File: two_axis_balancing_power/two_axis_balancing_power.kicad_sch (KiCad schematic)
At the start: 0 parts

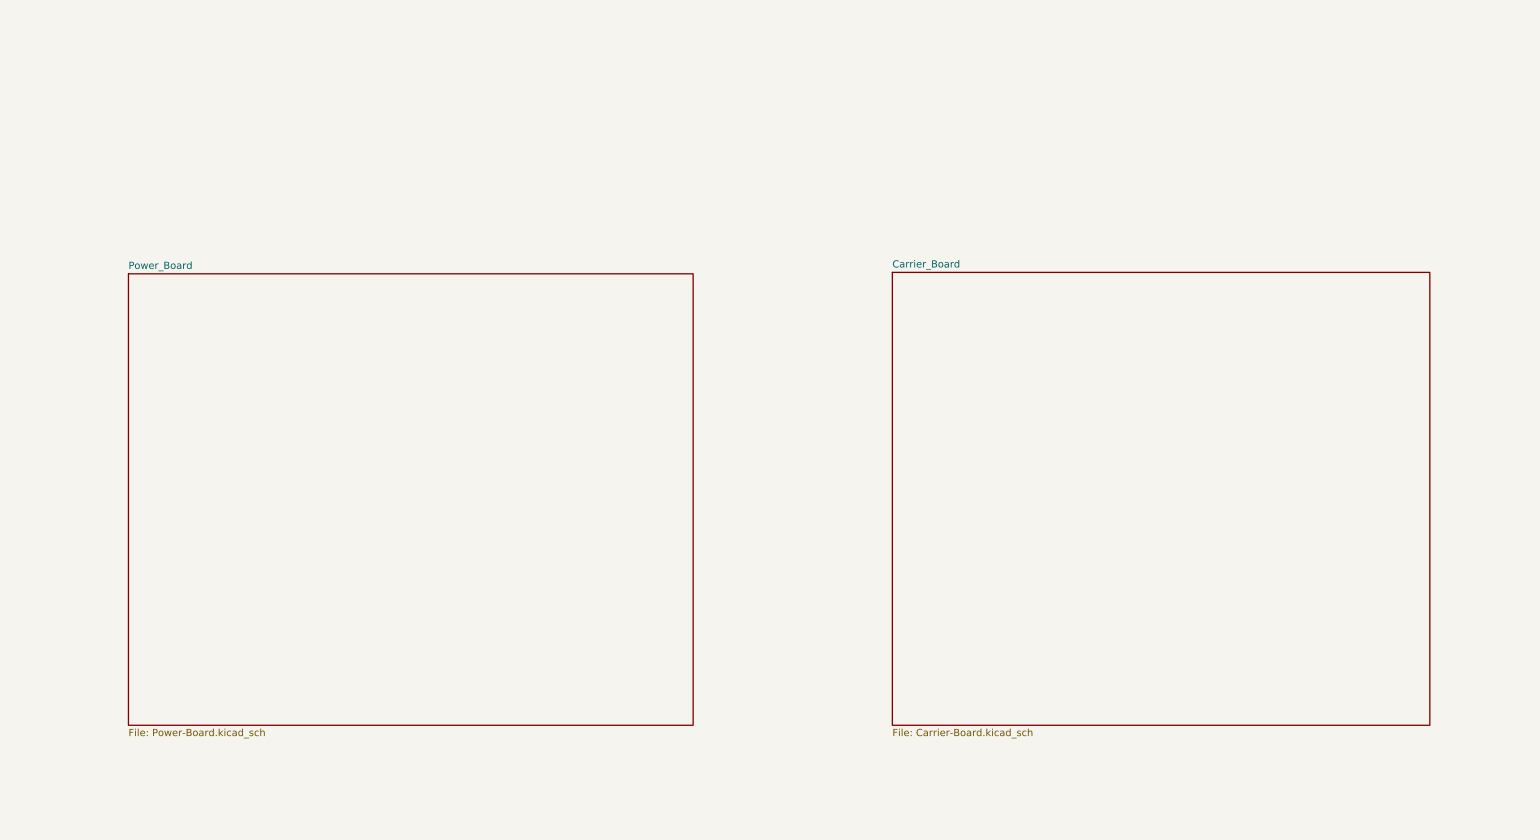
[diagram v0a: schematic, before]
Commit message: Fixed file structure
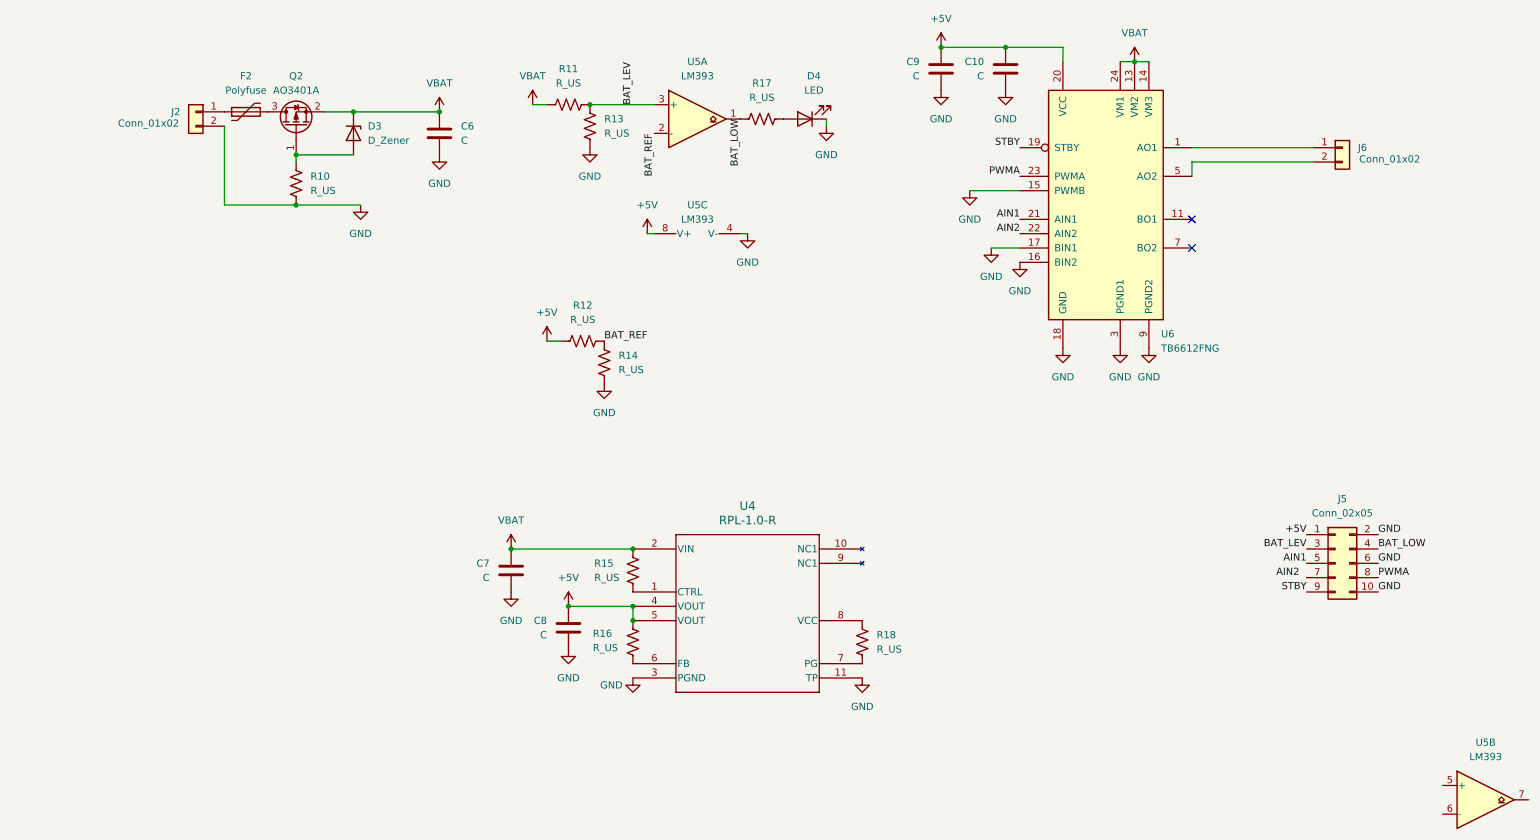
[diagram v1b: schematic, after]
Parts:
- added C10, C6, C7, C8, C9: C, symbol Device:C
- added D3: D_Zener, symbol Device:D_Zener
- added D4: LED, symbol Device:LED
- added F2: Polyfuse, symbol Device:Polyfuse
- added J2, J6: Conn_01x02, symbol Connector_Generic:Conn_01x02
- added J5: Conn_02x05, symbol Connector_Generic:Conn_02x05_Odd_Even
- added Q2: AO3401A, Package_TO_SOT_SMD:SOT-23, symbol Transistor_FET:AO3401A
- added R10, R11, R12, R13, R14, R15, R16, R17, R18: R_US, symbol Device:R_US
- added U4: RPL-1.0-R, 11L-LGA-M_RPL-1_RCP, symbol RPL_1.0:RPL-1.0-R
- added U5: LM393, symbol Comparator:LM393
- added U6: TB6612FNG, Package_SO:SSOP-24_5.3x8.2mm_P0.65mm, symbol Driver_Motor:TB6612FNG
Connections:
- new net: R16.1, U4.6 (FB)
- new net: R18.1, U4.8 (VCC)
- new net: R18.2, U4.7 (PG)
- new net: D4.2 (A), R17.1
- new net: R15.2, U4.1 (CTRL)
- new net: J6.1 (Pin_1), U6.1 (AO1), U6.2 (AO1)
- new net: U6.11 (BO1), U6.12 (BO1)
- new net: J6.2 (Pin_2), U6.5 (AO2), U6.6 (AO2)
- new net: U6.7 (BO2), U6.8 (BO2)
- new net: F2.1, J2.1 (Pin_1)
- new net: D3.2 (A), Q2.1 (G), R10.1
- new net: F2.2, Q2.3 (D)
- new net +5V: C10.2, C8.2, C9.2, J5.1 (Pin_1), R12.2, R16.2, U4.4 (VOUT), U4.5 (VOUT), U5.8 (V+), U6.20 (VCC)
- new net AIN1: J5.5 (Pin_5), U6.21 (AIN1)
- new net AIN2: U6.22 (AIN2)
- new net BAT_LEV: J5.3 (Pin_3), R11.1, R13.1, U5.3 (+)
- new net BAT_LOW: J5.4 (Pin_4), R17.2, U5.1
- new net BAT_REF: R12.1, R14.1, U5.2 (-)
- new net GND: C10.1, C6.2, C7.1, C8.1, C9.1, D4.1 (K), J2.2 (Pin_2), J5.10 (Pin_10), J5.2 (Pin_2), J5.6 (Pin_6), R10.2, R13.2, R14.2, U4.11 (TP), U4.3 (PGND), U5.4 (V-), U6.10 (PGND2), U6.15 (PWMB), U6.16 (BIN2), U6.17 (BIN1), U6.18 (GND), U6.3 (PGND1), U6.4 (PGND1), U6.9 (PGND2)
- new net PWMA: J5.8 (Pin_8), U6.23 (PWMA)
- new net STBY: J5.9 (Pin_9), U6.19 (STBY)
- new net VBAT: C6.1, C7.2, D3.1 (K), Q2.2 (S), R11.2, R15.1, U4.2 (VIN), U6.13 (VM2), U6.14 (VM3), U6.24 (VM1)
- no-connect marks 0 -> 2
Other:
- removed sheet Carrier_Board
- removed sheet Power_Board

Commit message: Finished topology
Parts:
- added J7: Conn_01x02, symbol Connector_Generic:Conn_01x02
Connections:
- net GND: now also J7.2 (Pin_2)
- net MOTOR_P: now reaches J6.1 (Pin_1), U6.1 (AO1), U6.2 (AO1)
- net MOTOR_N: now reaches J6.2 (Pin_2), U6.5 (AO2), U6.6 (AO2)
- net V_BAT_BYP: now reaches F2.1, J2.1 (Pin_1)
- net V_BAT_BYP: now also J7.1 (Pin_1)
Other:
- moved on the sheet: C6, D3, F2, J2, J5, J6, Q2, R10

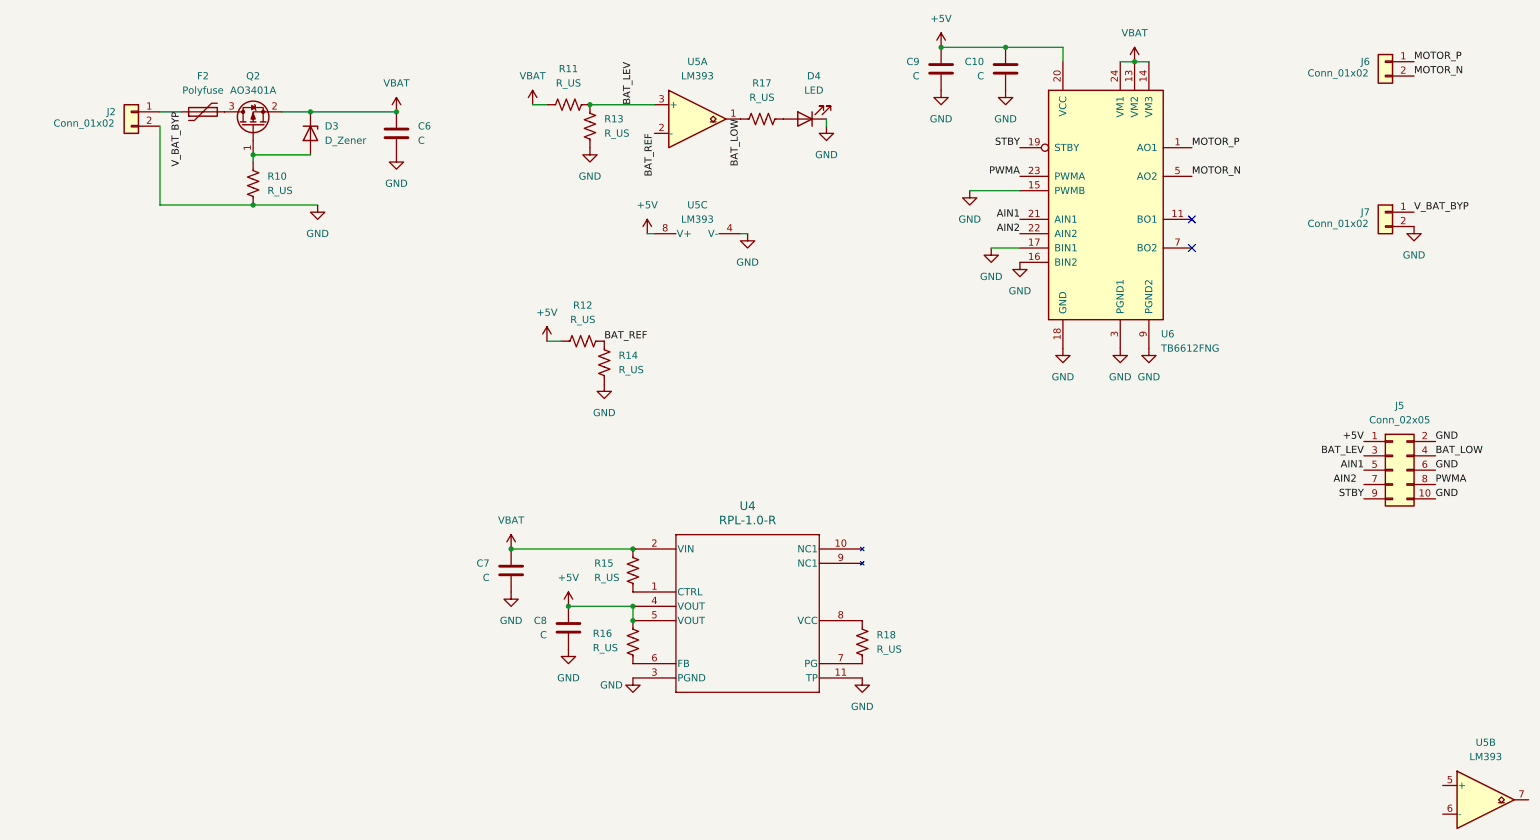
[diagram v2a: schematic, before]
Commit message: Sized passives
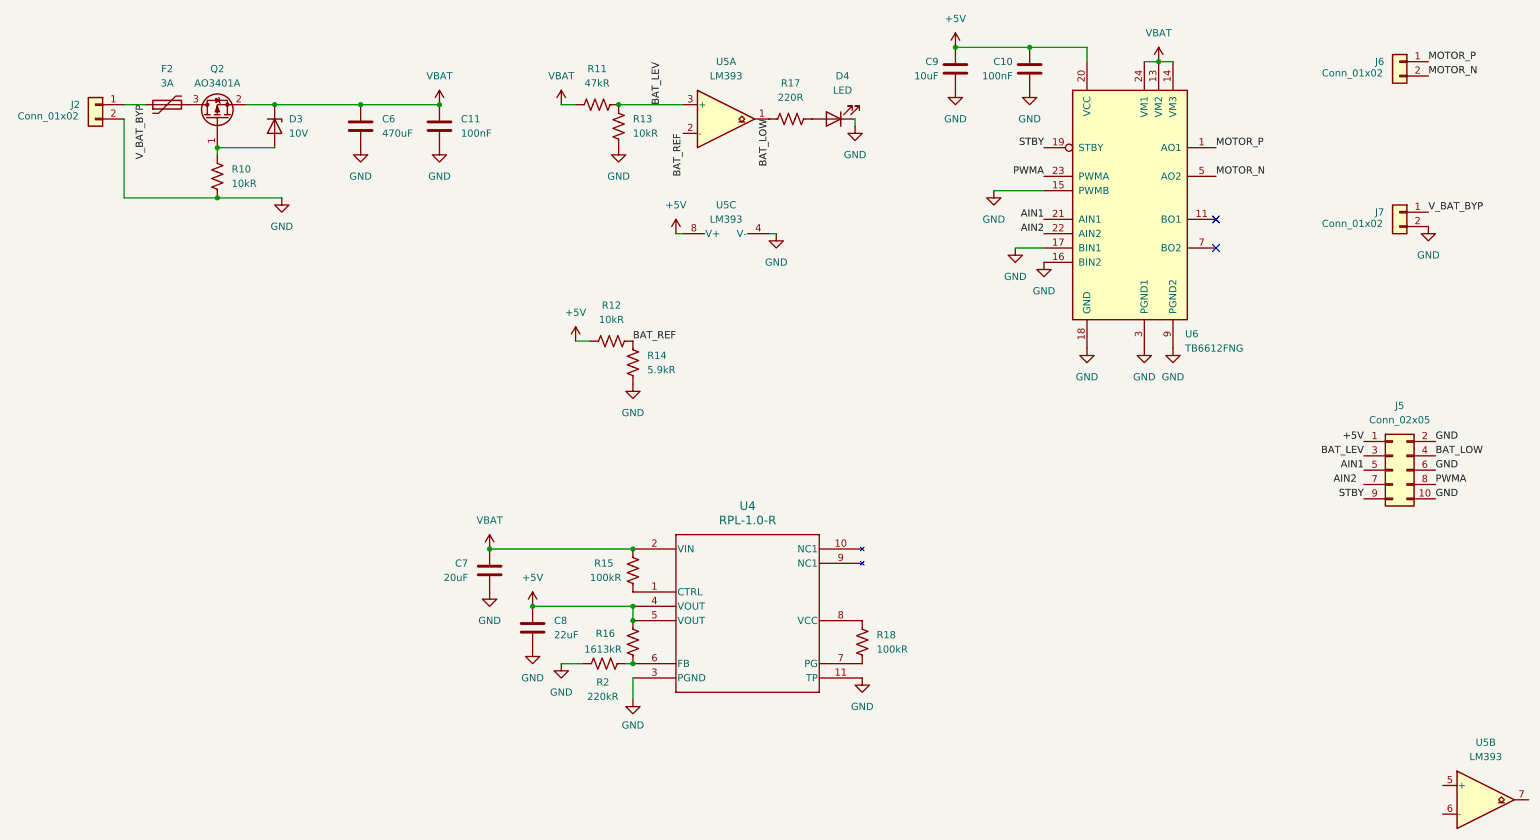
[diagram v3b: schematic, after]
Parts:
- added C11: 100nF, symbol Device:C
- added R2: 220kR, symbol Device:R_US
- C10: value C -> 100nF
- C6: value C -> 470uF
- C7: value C -> 20uF
- C8: value C -> 22uF
- C9: value C -> 10uF
- D3: value D_Zener -> 10V
- F2: value Polyfuse -> 3A
- R10, R12, R13: value R_US -> 10kR
- R11: value R_US -> 47kR
- R14: value R_US -> 5.9kR
- R15, R18: value R_US -> 100kR
- R16: value R_US -> 1613kR
- R17: value R_US -> 220R
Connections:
- net GND: now also C11.2, R2.1
- net VBAT: now also C11.1
- net at R16.1, U4.6 (FB): now also R2.2
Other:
- moved on the sheet: C10, C6, C7, C8, C9, D3, D4, F2, J2, J6, J7, Q2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

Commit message: Started pcb design
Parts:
- removed J7: Conn_01x02, symbol Connector_Generic:Conn_01x02
- C1: renamed from C6; footprint (none) -> Capacitor_SMD:C_0603_1608Metric
- C2: renamed from C11; footprint (none) -> Capacitor_SMD:C_0603_1608Metric
- C3: renamed from C7; footprint (none) -> Capacitor_SMD:C_0603_1608Metric
- C4: renamed from C8; footprint (none) -> Capacitor_SMD:C_0603_1608Metric
- C5: renamed from C9; footprint (none) -> Capacitor_SMD:C_0603_1608Metric
- C6: renamed from C10; footprint (none) -> Capacitor_SMD:C_0603_1608Metric
- D1: renamed from D3; footprint (none) -> Diode_SMD:D_SOD-123
- D2: renamed from D4; footprint (none) -> LED_SMD:LED_0603_1608Metric
- F1: renamed from F2; footprint (none) -> Fuse:Fuse_1812_4532Metric
- J1: renamed from J2; footprint (none) -> Connector_AMASS:AMASS_XT60-M_1x02_P7.20mm_Vertical
- J2: renamed from J5; footprint (none) -> Connector_IDC:IDC-Header_2x05_P2.54mm_Vertical
- J3: renamed from J6; footprint (none) -> Connector_JST:JST_XH_S2B-XH-A_1x02_P2.50mm_Horizontal
- R1: renamed from R10; footprint (none) -> Resistor_SMD:R_0603_1608Metric
- R10: renamed from R18; footprint (none) -> Resistor_SMD:R_0603_1608Metric
- R2: renamed from R11; footprint (none) -> Resistor_SMD:R_0603_1608Metric
- R3: renamed from R2; footprint (none) -> Resistor_SMD:R_0603_1608Metric
- R4: renamed from R12; footprint (none) -> Resistor_SMD:R_0603_1608Metric
- R5: renamed from R13; footprint (none) -> Resistor_SMD:R_0603_1608Metric
- R6: renamed from R14; footprint (none) -> Resistor_SMD:R_0603_1608Metric
- R7: renamed from R15; footprint (none) -> Resistor_SMD:R_0603_1608Metric
- R8: renamed from R16; footprint (none) -> Resistor_SMD:R_0603_1608Metric
- R9: renamed from R17; footprint (none) -> Resistor_SMD:R_0603_1608Metric
- U1: renamed from U4; footprint 11L-LGA-M_RPL-1_RCP -> RCL-1:11L-LGA-M_RPL-1_RCP
- U2: renamed from U5; footprint (none) -> Package_SO:SOIC-8_3.9x4.9mm_P1.27mm
- renumbered Q2 to Q1, U6 to U3
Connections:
- net AIN1: now also J2.8 (Pin_8); no longer J2.5 (Pin_5)
- net AIN2: now also J2.7 (Pin_7)
- net PWMA: now also J2.9 (Pin_9); no longer J2.8 (Pin_8)
- net STBY: now also J2.5 (Pin_5); no longer J2.9 (Pin_9)
- net V_BAT_BYP: no longer names the net of F1.1, J1.1 (Pin_1)
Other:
- moved on the sheet: J2

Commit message: Almost finished pcb
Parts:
- J2: footprint Connector_IDC:IDC-Header_2x05_P2.54mm_Vertical -> Connector_AMASS:AMASS_XT60-M_1x02_P7.20mm_Vertical
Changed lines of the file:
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@@
 			)
 		)
-		(property "Footprint" "Connector_IDC:IDC-Header_2x05_P2.54mm_Vertical"
+		(property "Footprint" "Connector_AMASS:AMASS_XT60-M_1x02_P7.20mm_Vertical"
 			(at 259.08 71.12 0)
 			(hide yes)

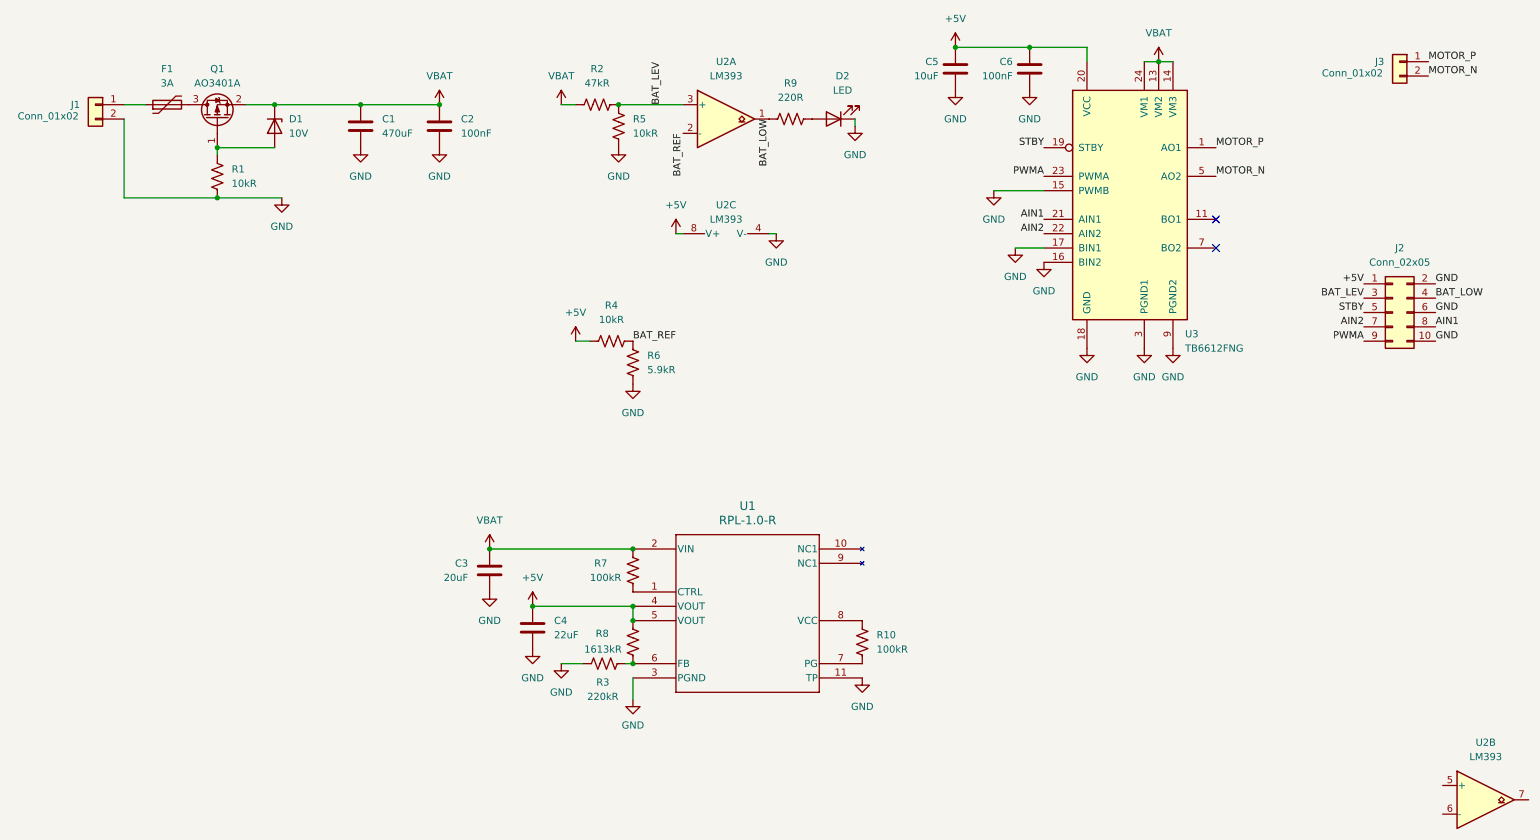
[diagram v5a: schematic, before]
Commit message: Power actually finished; carrier pcb started
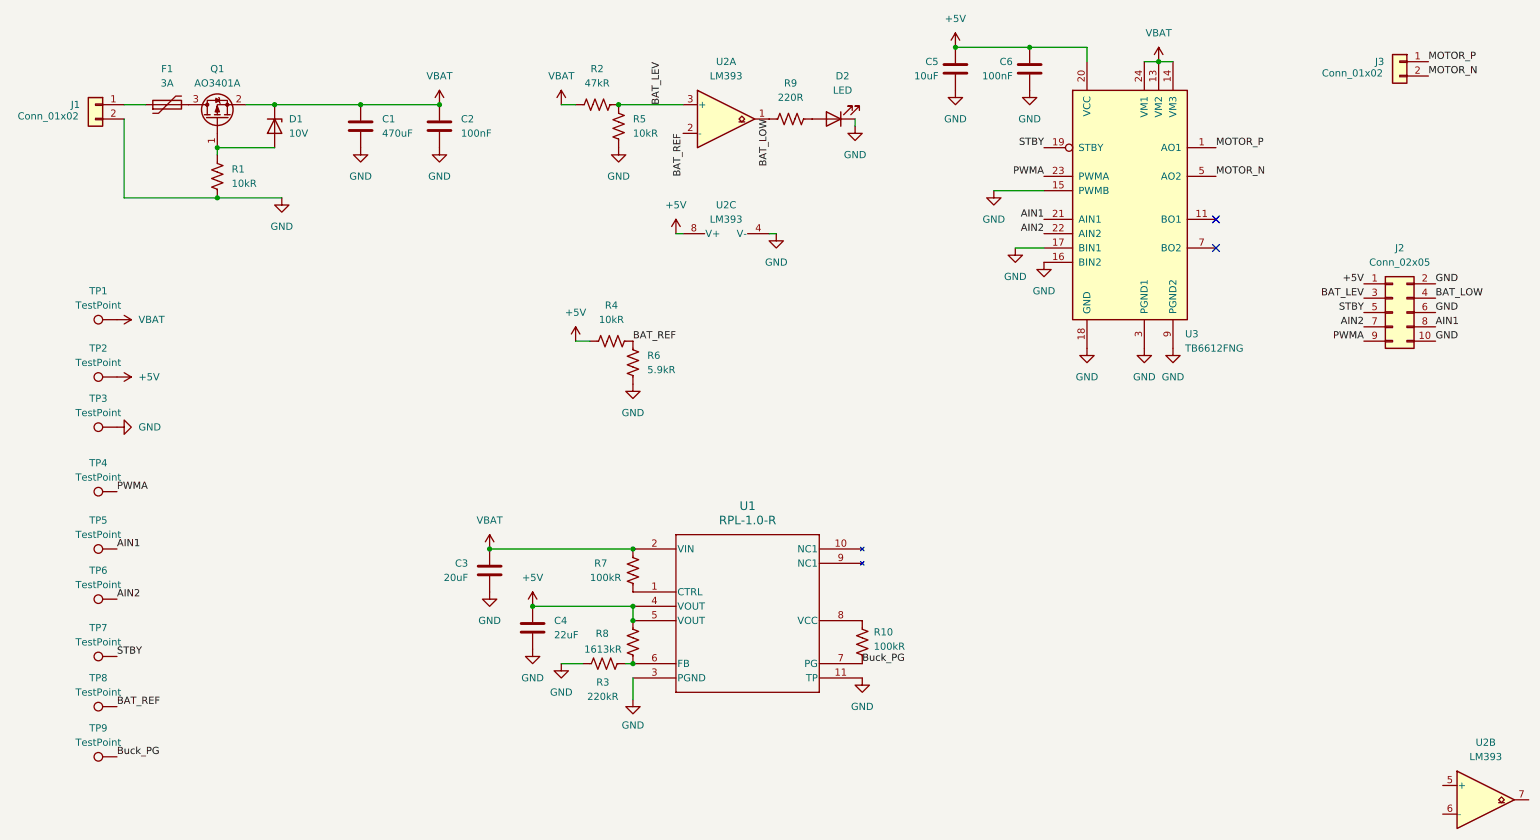
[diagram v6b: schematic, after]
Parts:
- added TP1, TP2, TP3, TP4, TP5, TP6, TP7, TP8, TP9: TestPoint, TestPoint:TestPoint_Pad_2.0x2.0mm, symbol Connector:TestPoint
- C1: footprint Capacitor_SMD:C_0603_1608Metric -> 470uF SMD:PCAP_10x10-ELECT_NCA
- C3: footprint Capacitor_SMD:C_0603_1608Metric -> Capacitor_SMD:C_1812_4532Metric
- C4: footprint Capacitor_SMD:C_0603_1608Metric -> Capacitor_SMD:C_0805_2012Metric
- J2: footprint Connector_AMASS:AMASS_XT60-M_1x02_P7.20mm_Vertical -> Connector_IDC:IDC-Header_2x05_P2.54mm_Vertical
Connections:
- net +5V: now also TP2.1
- net AIN1: now also TP5.1
- net AIN2: now also TP6.1
- net BAT_REF: now also TP8.1
- net GND: now also TP3.1
- net PWMA: now also TP4.1
- net STBY: now also TP7.1
- net VBAT: now also TP1.1
- net Buck_PG: now reaches R10.2, U1.7 (PG)
- net Buck_PG: now also TP9.1
